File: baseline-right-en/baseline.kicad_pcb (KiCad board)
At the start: 2 copper layers, 18 parts, among them J1 TYPE-C-31-M-12, SW1 TS-1088-AR02016, SW2 TS-1088-AR02016, U3 LD1117S33TR_SOT223

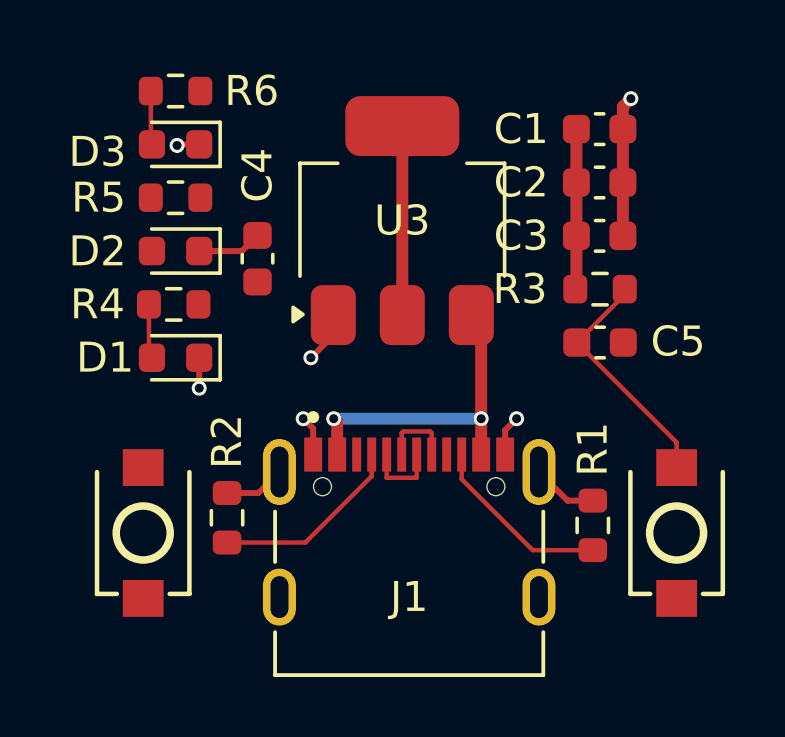
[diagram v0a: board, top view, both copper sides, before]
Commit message: baseline: tweak BOOT/EN button footprint silkscreen + re-save boards
Co-Authored-By: Claude Opus 4.8 (1M context) <noreply@anthropic.com>
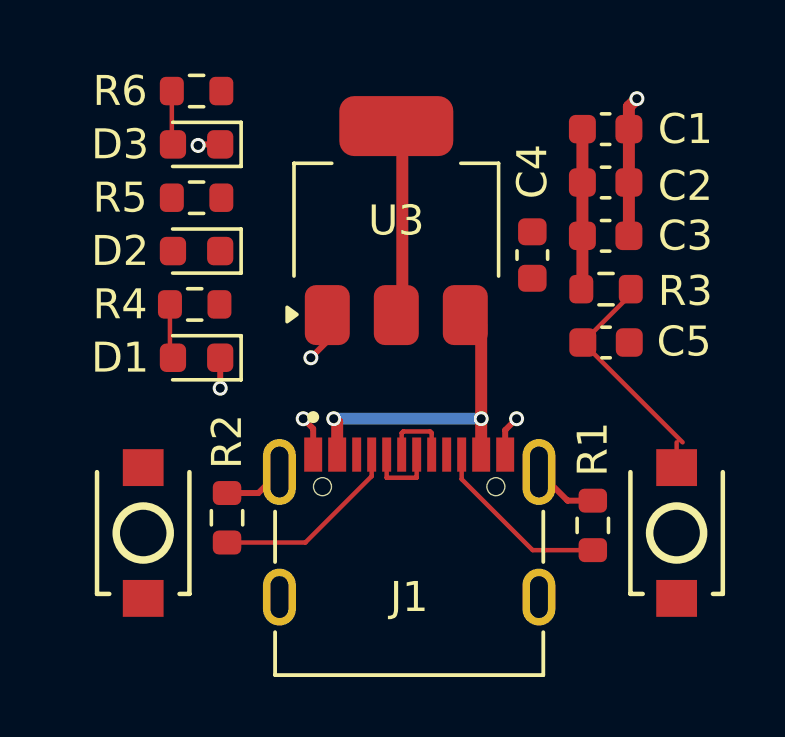
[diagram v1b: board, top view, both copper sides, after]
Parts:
- moved C4 9.16 mm to (164.1, 74.3)
- moved R4 0.70 mm to (152.8, 75.9)
- moved D1 0.70 mm to (152.9, 77.7)
- moved D2 0.70 mm to (152.9, 74.2)
- moved D3 0.70 mm to (152.9, 70.6)
- moved R5 0.70 mm to (152.9, 72.4)
- moved R6 0.70 mm to (152.9, 68.8)
- moved C1 0.20 mm to (166.5, 70.1)
- moved C2 0.20 mm to (166.5, 71.9)
- moved C3 0.20 mm to (166.5, 73.7)
- moved C5 0.20 mm to (166.6, 77.2)
- moved R3 0.20 mm to (166.6, 75.4)
- moved U3 0.20 mm to (159.6, 73.2)
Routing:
- net GND: track 17.6 -> 15.4 mm
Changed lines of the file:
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@@
 		(capping no)
 		(filling no)
-		(zone_defaults)
 		(pcbplotparams
 			(layerselection 0x00000000_00000000_55555555_5755f5ff)
@@
 	(footprint "Capacitor_SMD:C_0603_1608Metric"
 		(layer "F.Cu")
-		(at 166.357 77.216)
+		(at 166.557 77.216)
 		(descr "Capacitor SMD 0603 (1608 Metric), square (rectangular) end terminal, IPC-7351 nominal, (Body size source: IPC-SM-782 page 76, https://www.pcb-3d.com/wordpress/wp-content/uploads/ipc-sm-782a_amendment_1_and_2.pdf)")
 		(tags "capacitor")
@@
 	(footprint "Capacitor_SMD:C_0603_1608Metric"
 		(layer "F.Cu")
-		(at 166.344 73.66)
+		(at 166.544 73.66)
 		(descr "Capacitor SMD 0603 (1608 Metric), square (rectangular) end terminal, IPC-7351 nominal, (Body size source: IPC-SM-782 page 76, https://www.pcb-3d.com/wordpress/wp-content/uploads/ipc-sm-782a_amendment_1_and_2.pdf)")
 		(tags "capacitor")
 		(property "Reference" "C3"
-			(at -2.616 0 0)
+			(at 2.656 0 0)
 			(layer "F.SilkS")
 			(effects
@@
 	(footprint "Resistor_SMD:R_0603_1608Metric"
 		(layer "F.Cu")
-		(at 152.209 72.39 180)
+		(at 152.909 72.39 180)
 		(descr "Resistor SMD 0603 (1608 Metric), square (rectangular) end terminal, IPC-7351 nominal, (Body size source: IPC-SM-782 page 72, https://www.pcb-3d.com/wordpress/wp-content/uploads/ipc-sm-782a_amendment_1_and_2.pdf)")
 		(tags "resistor")
 		(property "Reference" "R5"
-			(at 2.5655 0 0)
+			(at 2.549 0 0)
 			(layer "F.SilkS")
 			(effects
@@
 	(footprint "Capacitor_SMD:C_0603_1608Metric"
 		(layer "F.Cu")
-		(at 166.344 71.882)
+		(at 166.544 71.882)
 		(descr "Capacitor SMD 0603 (1608 Metric), square (rectangular) end terminal, IPC-7351 nominal, (Body size source: IPC-SM-782 page 76, https://www.pcb-3d.com/wordpress/wp-content/uploads/ipc-sm-782a_amendment_1_and_2.pdf)")
 		(tags "capacitor")
 		(property "Reference" "C2"
-			(at -2.616 0 0)
+			(at 2.656 0.118 0)
 			(layer "F.SilkS")
 			(effects
@@
 	(footprint "Resistor_SMD:R_0603_1608Metric"
 		(layer "F.Cu")
-		(at 152.146 75.946 180)
+		(at 152.846 75.946 180)
 		(descr "Resistor SMD 0603 (1608 Metric), square (rectangular) end terminal, IPC-7351 nominal, (Body size source: IPC-SM-782 page 72, https://www.pcb-3d.com/wordpress/wp-content/uploads/ipc-sm-782a_amendment_1_and_2.pdf)")
 		(tags "resistor")
 		(property "Reference" "R4"
-			(at 2.54 0 0)
+			(at 2.486 0 0)
 			(layer "F.SilkS")
 			(effects
@@
 	(footprint "Resistor_SMD:R_0603_1608Metric"
 		(layer "F.Cu")
-		(at 152.209 68.834 180)
+		(at 152.909 68.834 180)
 		(descr "Resistor SMD 0603 (1608 Metric), square (rectangular) end terminal, IPC-7351 nominal, (Body size source: IPC-SM-782 page 72, https://www.pcb-3d.com/wordpress/wp-content/uploads/ipc-sm-782a_amendment_1_and_2.pdf)")
 		(tags "resistor")
 		(property "Reference" "R6"
-			(at -2.54 0 0)
+			(at 2.549 0 0)
 			(layer "F.SilkS")
 			(effects
@@
 		(sheetname "/")
 		(sheetfile "baseline.kicad_sch")
-		(units
-			(unit
-				(name "A")
-				(pins "1" "2")
-			)
-		)
 		(attr smd)
 		(duplicate_pad_numbers_are_jumpers no)
@@
 		(fp_line
 			(start -2.03 -1.54)
-			(end -2.03 -0.88)
+			(end -2.03 -1.13)
 			(stroke
 				(width 0.15)
@@
 		(fp_line
 			(start -2.03 1.54)
-			(end -2.03 0.88)
+			(end -2.03 1.21)
 			(stroke
 				(width 0.15)
@@
 	(footprint "Capacitor_SMD:C_0603_1608Metric"
 		(layer "F.Cu")
-		(at 154.94 74.422 90)
+		(at 164.1 74.3 90)
 		(descr "Capacitor SMD 0603 (1608 Metric), square (rectangular) end terminal, IPC-7351 nominal, (Body size source: IPC-SM-782 page 76, https://www.pcb-3d.com/wordpress/wp-content/uploads/ipc-sm-782a_amendment_1_and_2.pdf)")
 		(tags "capacitor")
@@
 	(footprint "Package_TO_SOT_SMD:SOT-223-3_TabPin2"
 		(layer "F.Cu")
-		(at 159.766 73.152 90)
+		(at 159.566 73.152 90)
 		(descr "module CMS SOT223 4 pins")
 		(tags "CMS SOT")
@@
 	(footprint "Resistor_SMD:R_0603_1608Metric"
 		(layer "F.Cu")
-		(at 166.357 75.438)
+		(at 166.557 75.438)
 		(descr "Resistor SMD 0603 (1608 Metric), square (rectangular) end terminal, IPC-7351 nominal, (Body size source: IPC-SM-782 page 72, https://www.pcb-3d.com/wordpress/wp-content/uploads/ipc-sm-782a_amendment_1_and_2.pdf)")
 		(tags "resistor")
 		(property "Reference" "R3"
-			(at -2.666 0 0)
+			(at 2.643 0.062 0)
 			(layer "F.SilkS")
 			(effects
@@
 	(footprint "LED_SMD:LED_0603_1608Metric"
 		(layer "F.Cu")
-		(at 152.209 77.724 180)
+		(at 152.909 77.724 180)
 		(descr "LED SMD 0603 (1608 Metric), square (rectangular) end terminal, IPC-7351 nominal, (Body size source: http://www.tortai-tech.com/upload/download/2011102023233369053.pdf)")
 		(tags "LED")
 		(property "Reference" "D1"
-			(at 2.349 0 0)
+			(at 2.549 0 0)
 			(layer "F.SilkS")
 			(effects
@@
 	(footprint "LED_SMD:LED_0603_1608Metric"
 		(layer "F.Cu")
-		(at 152.209 70.612 180)
+		(at 152.909 70.612 180)
 		(descr "LED SMD 0603 (1608 Metric), square (rectangular) end terminal, IPC-7351 nominal, (Body size source: http://www.tortai-tech.com/upload/download/2011102023233369053.pdf)")
 		(tags "LED")
 		(property "Reference" "D3"
-			(at 2.603 -0.254 0)
+			(at 2.549 0 0)
 			(layer "F.SilkS")
 			(effects
@@
 	(footprint "Capacitor_SMD:C_0603_1608Metric"
 		(layer "F.Cu")
-		(at 166.344 70.104)
+		(at 166.544 70.104)
 		(descr "Capacitor SMD 0603 (1608 Metric), square (rectangular) end terminal, IPC-7351 nominal, (Body size source: IPC-SM-782 page 76, https://www.pcb-3d.com/wordpress/wp-content/uploads/ipc-sm-782a_amendment_1_and_2.pdf)")
 		(tags "capacitor")
 		(property "Reference" "C1"
-			(at -2.616 0 0)
+			(at 2.656 0 0)
 			(layer "F.SilkS")
 			(effects
@@
 	(footprint "LED_SMD:LED_0603_1608Metric"
 		(layer "F.Cu")
-		(at 152.209 74.168 180)
+		(at 152.909 74.168 180)
 		(descr "LED SMD 0603 (1608 Metric), square (rectangular) end terminal, IPC-7351 nominal, (Body size source: http://www.tortai-tech.com/upload/download/2011102023233369053.pdf)")
 		(tags "LED")
 		(property "Reference" "D2"
-			(at 2.603 -0.013 0)
+			(at 2.549 0 0)
 			(layer "F.SilkS")
 			(effects
@@
 		(sheetname "/")
 		(sheetfile "baseline.kicad_sch")
-		(units
-			(unit
-				(name "A")
-				(pins "1" "2")
-			)
-		)
 		(attr smd)
 		(duplicate_pad_numbers_are_jumpers no)
@@
 		(fp_line
 			(start -2.03 -1.54)
-			(end -2.03 -0.88)
+			(end -2.03 -1.13)
 			(stroke
 				(width 0.15)
@@
 		(fp_line
 			(start -2.03 1.54)
-			(end -2.03 0.88)
+			(end -2.03 1.21)
 			(stroke
 				(width 0.15)
@@
 	)
 	(segment
-		(start 167.182 75.438)
-		(end 167.182 75.616)
+		(start 167.382 75.438)
+		(end 167.382 75.616)
 		(width 0.15)
 		(layer "F.Cu")
@@
 	)
 	(segment
-		(start 167.182 75.616)
-		(end 165.582 77.216)
+		(start 167.382 75.616)
+		(end 165.782 77.216)
 		(width 0.15)
 		(layer "F.Cu")
@@
 	)
 	(segment
-		(start 168.91 80.544)
-		(end 165.582 77.216)
+		(start 169.11 80.544)
+		(end 165.782 77.216)
 		(width 0.15)
 		(layer "F.Cu")
@@
 	)
 	(segment
-		(start 167.271 70.256)
-		(end 167.119 70.104)
+		(start 167.471 70.256)
+		(end 167.319 70.104)
 		(width 0.2)
 		(layer "F.Cu")
@@
 	)
 	(segment
-		(start 152.293547 70.612)
-		(end 152.259 70.646547)
+		(start 152.993547 70.612)
+		(end 152.959 70.646547)
 		(width 0.2)
 		(layer "F.Cu")
@@
 	)
 	(segment
-		(start 167.119 73.66)
-		(end 167.119 69.355)
+		(start 167.319 73.66)
+		(end 167.319 69.355)
 		(width 0.4)
 		(layer "F.Cu")
@@
 	)
 	(segment
-		(start 167.182 70.167)
-		(end 167.119 70.104)
+		(start 167.382 70.167)
+		(end 167.319 70.104)
 		(width 0.2)
 		(layer "F.Cu")
@@
 	)
 	(segment
-		(start 152.9965 70.612)
-		(end 152.293547 70.612)
+		(start 153.6965 70.612)
+		(end 152.993547 70.612)
 		(width 0.2)
 		(layer "F.Cu")
@@
 	)
 	(segment
-		(start 152.9965 74.168)
-		(end 154.419 74.168)
-		(width 0.2)
-		(layer "F.Cu")
-		(net "GND")
-	)
-	(segment
 		(start 163.1955 80.1365)
 		(end 163.576 79.756)
@@
 	)
 	(segment
-		(start 152.9965 77.724)
-		(end 152.9965 78.74)
+		(start 153.6965 77.724)
+		(end 153.6965 78.74)
 		(width 0.2)
 		(layer "F.Cu")
@@
 	)
 	(segment
-		(start 167.119 69.355)
-		(end 167.386 69.088)
+		(start 167.319 69.355)
+		(end 167.586 69.088)
 		(width 0.4)
 		(layer "F.Cu")
@@
 	)
 	(segment
-		(start 154.419 74.168)
-		(end 154.94 73.647)
-		(width 0.2)
-		(layer "F.Cu")
-		(net "GND")
-	)
-	(segment
 		(start 154.9695 82.233)
 		(end 155.6705 81.532)
@@
 	)
 	(via
-		(at 152.259 70.646547)
+		(at 152.959 70.646547)
 		(size 0.5)
 		(drill 0.3)
@@
 	)
 	(via
-		(at 152.9965 78.74)
+		(at 153.6965 78.74)
 		(size 0.5)
 		(drill 0.3)
@@
 	)
 	(via
-		(at 167.386 69.088)
+		(at 167.586 69.088)
 		(size 0.5)
 		(drill 0.3)
@@
 	)
 	(segment
-		(start 165.569 70.104)
-		(end 165.569 75.401)
+		(start 165.769 70.104)
+		(end 165.769 75.401)
 		(width 0.4)
 		(layer "F.Cu")
@@
 	)
 	(segment
-		(start 165.582 75.488)
-		(end 165.532 75.438)
+		(start 165.782 75.488)
+		(end 165.732 75.438)
 		(width 0.15)
 		(layer "F.Cu")
@@
 	)
 	(segment
-		(start 153.034 72.39)
-		(end 153.034 72.5555)
+		(start 153.734 72.39)
+		(end 153.734 72.5555)
 		(width 0.15)
 		(layer "F.Cu")
@@
 	)
 	(segment
-		(start 165.569 75.401)
-		(end 165.532 75.438)
+		(start 165.769 75.401)
+		(end 165.732 75.438)
 		(width 0.4)
 		(layer "F.Cu")
@@
 	)
 	(segment
-		(start 151.321 77.6235)
-		(end 151.4215 77.724)
+		(start 152.021 77.6235)
+		(end 152.1215 77.724)
 		(width 0.15)
 		(layer "F.Cu")
@@
 	)
 	(segment
-		(start 151.321 75.946)
-		(end 151.321 77.6235)
+		(start 152.021 75.946)
+		(end 152.021 77.6235)
 		(width 0.15)
 		(layer "F.Cu")
@@
 	)
 	(segment
-		(start 151.384 70.5745)
-		(end 151.4215 70.612)
+		(start 152.084 70.5745)
+		(end 152.1215 70.612)
 		(width 0.15)
 		(layer "F.Cu")
@@
 	)
 	(segment
-		(start 151.384 68.834)
-		(end 151.384 70.5745)
+		(start 152.084 68.834)
+		(end 152.084 70.5745)
 		(width 0.15)
 		(layer "F.Cu")
